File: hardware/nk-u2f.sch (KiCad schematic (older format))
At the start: 22 parts, among them J1 USB_Plug, P1 TouchPAD, U1 EFM8UB1xFxxG-QFN20, U2 MTCH101, U3 DF5A5.6JE, U4 ATECC508A

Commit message: Add files via upload
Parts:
- added C4: 0.1uF, Capacitors_SMD:C_0402, symbol C
- added R4, R5, R6, R7, R8: 4K7, Resistors_SMD:R_0402, symbol R
- renumbered GND1 to TP1, D+1 to TP2, D-1 to TP3, +5V1 to TP4, C2CK1 to TP5, C2D1 to TP6, GND2 to TP7, RX1 to TP8, TX1 to TP9
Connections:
- net labels added: Button_reset
- wire segments 51 -> 65
- no-connect marks 11 -> 10
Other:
- note added: "Debugging Pins\n\n"
- moved on the sheet: TP1, TP2, TP3, TP4, TP5, TP6, TP7, TP8, TP9

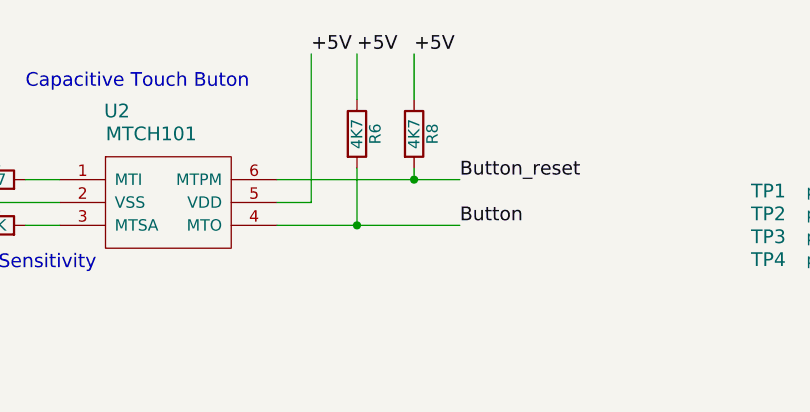
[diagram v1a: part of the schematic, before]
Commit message: REV4
R6, R8, and their tracks have been deleted.
GND planes refilled.
TOP, BOT pdfs have been refreshed.
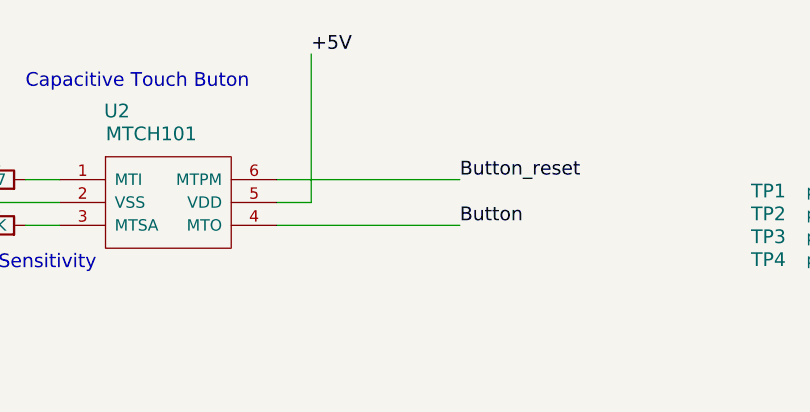
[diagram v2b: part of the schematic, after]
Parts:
- removed R6, R8: 4K7, Resistors_SMD:R_0402, symbol R
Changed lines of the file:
@@
 Secure element for EC
 $Comp
-L PWR_FLAG-RESCUE-nk-u2f #FLG2
+L PWR_FLAG-RESCUE-nk-u2f #FLG01
 U 1 1 5686E60B
 P 9650 5800
-F 0 "#FLG2" H 9650 5895 50  0001 C CNN
+F 0 "#FLG01" H 9650 5895 50  0001 C CNN
 F 1 "PWR_FLAG" H 9650 5980 50  0000 C CNN
 F 2 "" H 9650 5800 50  0000 C CNN
@@
 Wire Wire Line
 	5200 1800 5100 1800
-Text Label 6750 1050 0    60   ~ 0
-+5V
 $Comp
 L C C1
@@
 Wire Wire Line
 	5100 1800 5100 1700
-$Comp
-L R R6
-U 1 1 5A7781E8
-P 6950 1400
-F 0 "R6" V 7030 1400 50  0000 C CNN
-F 1 "4K7" V 6950 1400 50  0000 C CNN
-F 2 "Resistors_SMD:R_0402" V 6880 1400 50  0001 C CNN
-F 3 "http://www.vishay.com/docs/20035/dcrcwe3.pdf" H 6950 1400 50  0001 C CNN
-F 4 "Vishay Dale" H 6950 1400 60  0001 C CNN "MFG Name"
-F 5 "?" H 6950 1400 60  0001 C CNN "MFG Part Num"
-F 6 "?" H 6950 1400 60  0001 C CNN "Distributer PN"
-F 7 "?" H 6950 1400 60  0001 C CNN "Distributer Link"
-	1    6950 1400
-	1    0    0    -1
-$EndComp
 Text Label 7400 1600 0    60   ~ 0
 Button_reset
 Wire Wire Line
 	6750 1700 6750 1050
-Wire Wire Line
-	6950 1250 6950 1050
-Text Label 6950 1050 0    60   ~ 0
-+5V
-$Comp
-L R R8
-U 1 1 5A778805
-P 7200 1400
-F 0 "R8" V 7280 1400 50  0000 C CNN
-F 1 "4K7" V 7200 1400 50  0000 C CNN
-F 2 "Resistors_SMD:R_0402" V 7130 1400 50  0001 C CNN
-F 3 "http://www.vishay.com/docs/20035/dcrcwe3.pdf" H 7200 1400 50  0001 C CNN
-F 4 "Vishay Dale" H 7200 1400 60  0001 C CNN "MFG Name"
-F 5 "?" H 7200 1400 60  0001 C CNN "MFG Part Num"
-F 6 "?" H 7200 1400 60  0001 C CNN "Distributer PN"
-F 7 "?" H 7200 1400 60  0001 C CNN "Distributer Link"
-	1    7200 1400
-	1    0    0    -1
-$EndComp
-Wire Wire Line
-	7200 1250 7200 1050
-Text Label 7200 1050 0    60   ~ 0
-+5V
-Wire Wire Line
-	7200 1550 7200 1600
-Connection ~ 7200 1600
-Wire Wire Line
-	6950 1550 6950 1800
-Connection ~ 6950 1800
 $Comp
 L R R4
@@
 +5V
 $Comp
-L PWR_FLAG-RESCUE-nk-u2f #FLG1
+L PWR_FLAG-RESCUE-nk-u2f #FLG02
 U 1 1 5A77BCD6
 P 9250 5800
-F 0 "#FLG1" H 9250 5895 50  0001 C CNN
+F 0 "#FLG02" H 9250 5895 50  0001 C CNN
 F 1 "PWR_FLAG" H 9250 5980 50  0000 C CNN
 F 2 "" H 9250 5800 50  0000 C CNN
@@
 Text Notes 10050 2400 2    60   ~ 0
 Debugging Pins\n\n
+Text Label 6750 1050 0    60   ~ 0
++5V
 $EndSCHEMATC

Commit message: REV5: - debug uart pads deleted - mcu replaced with EFM8UB30F40G-A-QFN20 (program memory upgrade 16->40kB)
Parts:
- removed TP7, TP8, TP9: debug-pin, footprints:Prog_Pad, symbol debug-pin
- U1: value EFM8UB1xFxxG-QFN20 -> EFM8UB30F40G-A; symbol EFM8UB1xFxxG-QFN20 -> EFM8UBx-QFN20
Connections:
- net RX: no longer names the net of U1.17 (P0.5/RX)
- net TX: no longer names the net of U1.18 (P0.4/TX)
- no-connect marks 10 -> 12
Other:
- note removed: "Debugging Pins\n\n"
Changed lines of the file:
@@
 Sheet 1 1
 Title "Nitrokey FIDO U2F"
-Date "2018-01-29"
-Rev "R3"
+Date "2018-05-23"
+Rev "R5"
 Comp "Nitrokey"
 Comment1 ""
@@
 C2D
 $Comp
-L debug-pin TP9
-U 1 1 56A3F7EB
-P 9950 2850
-F 0 "TP9" V 9750 2300 60  0000 C CNN
-F 1 "debug-pin" H 10050 2600 60  0001 C CNN
-F 2 "footprints:Prog_Pad" H 9950 2850 60  0001 C CNN
-F 3 "" H 9950 2850 60  0000 C CNN
-	1    9950 2850
-	0    1    1    0
-$EndComp
-$Comp
-L debug-pin TP8
-U 1 1 56A3F89E
-P 9950 2750
-F 0 "TP8" V 9750 2200 60  0000 C CNN
-F 1 "debug-pin" H 10050 2500 60  0001 C CNN
-F 2 "footprints:Prog_Pad" H 9950 2750 60  0001 C CNN
-F 3 "" H 9950 2750 60  0000 C CNN
-	1    9950 2750
-	0    1    1    0
-$EndComp
-$Comp
 L debug-pin TP5
 U 1 1 56A3F8D6
@@
 	0    -1   -1   0
 $EndComp
-Text Label 9800 2650 0    60   ~ 0
-TX
-Text Label 9800 2550 0    60   ~ 0
-RX
 NoConn ~ 1500 1400
 Text Label 3050 1200 0    60   ~ 0
@@
 	4950 6500 4650 6500
 $Comp
-L EFM8UB1xFxxG-QFN20 U1
+L EFM8UBx-QFN20 U1
 U 1 1 58B4B07B
 P 6000 4400
 F 0 "U1" H 5500 5100 60  0000 C CNN
-F 1 "EFM8UB1xFxxG-QFN20" H 5150 5250 60  0000 C CNN
+F 1 "EFM8UB30F40G-A" H 5150 5250 60  0000 C CNN
 F 2 "footprints:QFN-20-0.5mm-user" H 5800 4450 60  0001 C CNN
 F 3 "" H 5800 4450 60  0001 C CNN
@@
 Text Label 6200 3100 1    60   ~ 0
 LED
-Wire Wire Line
-	6100 3600 6100 3100
-Wire Wire Line
-	6000 3600 6000 3100
-Text Label 6000 3100 1    60   ~ 0
-TX
-Text Label 6100 3100 1    60   ~ 0
-RX
 Wire Wire Line
 	5250 4200 4700 4200
@@
 Text Label 9200 1950 0    60   ~ 0
 +5V
-$Comp
-L debug-pin TP7
-U 1 1 58BF71CE
-P 9950 2650
-F 0 "TP7" V 9750 2100 60  0000 C CNN
-F 1 "debug-pin" H 10050 2400 60  0001 C CNN
-F 2 "footprints:Prog_Pad" H 9650 2750 60  0001 C CNN
-F 3 "" H 9950 2650 60  0000 C CNN
-	1    9950 2650
-	0    1    1    0
-$EndComp
-Text Label 9800 2450 0    60   ~ 0
-GND
 Wire Wire Line
 	5100 1800 5100 1700
@@
 	-1   0    0    1
 $EndComp
-Text Notes 10050 2400 2    60   ~ 0
-Debugging Pins\n\n
 Text Label 6750 1050 0    60   ~ 0
 +5V
+NoConn ~ 6000 3600
+NoConn ~ 6100 3600
 $EndSCHEMATC
